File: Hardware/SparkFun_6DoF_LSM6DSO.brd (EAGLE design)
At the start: 25.4 x 25.4 mm, 62 parts, among them J1 QWIIC_RIGHT_ANGLE, J2 QWIIC_RIGHT_ANGLE, U1 LSM6DS0

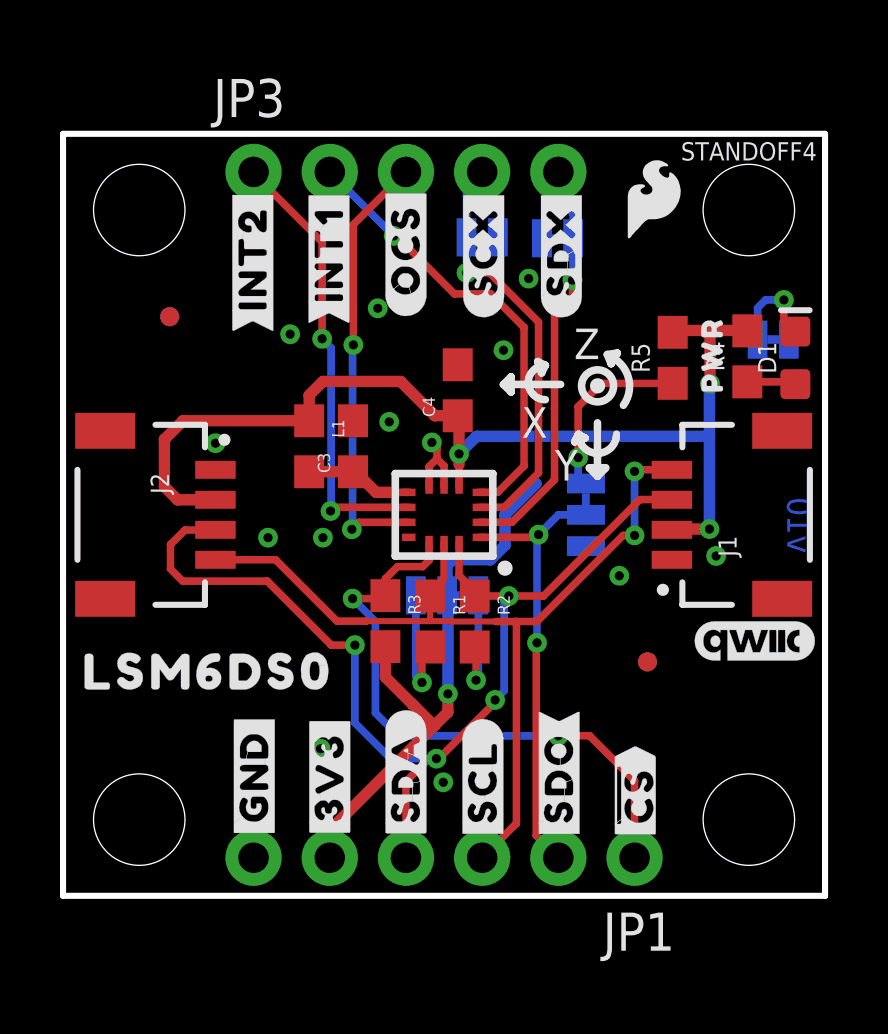
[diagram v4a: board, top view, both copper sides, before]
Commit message: Updates IC with production ID, adjusts connector section
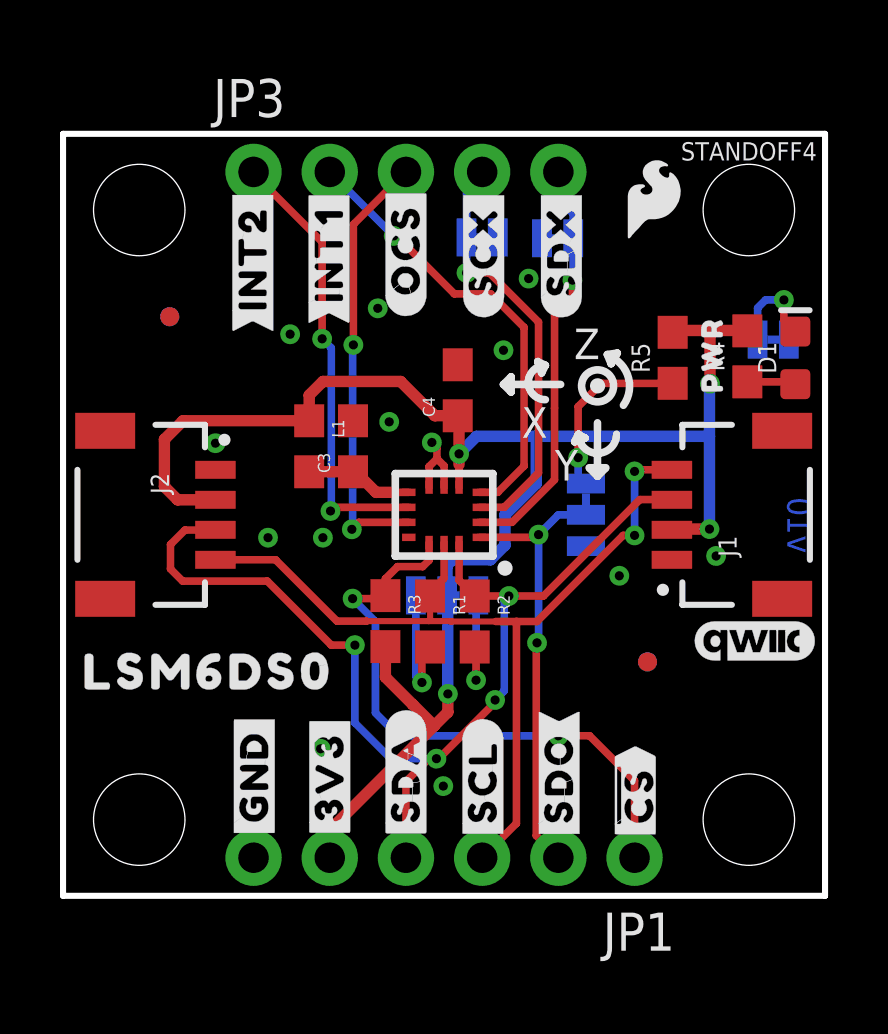
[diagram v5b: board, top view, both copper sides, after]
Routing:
- net 3.3V: track 56.1 -> 57.7 mm
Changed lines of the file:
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@@
 <setting verticaltext="up"/>
 </settings>
-<grid distance="0.05" unitdist="inch" unit="inch" style="dots" multiple="1" display="yes" altdistance="0.005" altunitdist="inch" altunit="inch"/>
+<grid distance="0.01" unitdist="inch" unit="inch" style="dots" multiple="1" display="yes" altdistance="0.001" altunitdist="inch" altunit="inch"/>
 <layers>
 <layer number="1" name="Top" color="4" fill="1" visible="yes" active="yes"/>
@@
 <element name="U1" library="temp" package="LGA14L" value="LSM6DS0" x="12.7" y="12.7" smashed="yes" rot="R180">
 <attribute name="NAME" x="14.057" y="10.928" size="0.6096" layer="27" font="vector" ratio="20" rot="R180"/>
+<attribute name="PROD_ID" value="IC-15837" x="12.7" y="12.7" size="1.778" layer="27" rot="R180" display="off"/>
 <attribute name="VALUE" x="14.311" y="15.091" size="0.6096" layer="27" font="vector" ratio="20" rot="R180"/>
 </element>
@@
 <wire x1="12.4634" y1="14.57056875" x2="12.4634" y2="14.9432" width="0.254" layer="1"/>
 <wire x1="12.4634" y1="14.9432" x2="12.2936" y2="15.113" width="0.254" layer="1"/>
-<via x="12.6746" y="3.7846" extent="1-16" drill="0.3048"/>
+<via x="12.6746" y="3.6576" extent="1-16" drill="0.3048"/>
 </signal>
 <signal name="VDD">
@@
 <wire x1="12.7" y1="10.58455" x2="12.23645" y2="10.121" width="0.254" layer="1"/>
 <wire x1="12.23645" y1="10.121" x2="12.23645" y2="9.994" width="0.254" layer="1"/>
-<wire x1="9.1322" y1="9.1558" x2="10.11225" y2="9.1558" width="0.254" layer="1"/>
-<wire x1="10.11225" y1="9.1558" x2="10.11315" y2="9.1567" width="0.254" layer="1"/>
 <wire x1="12.9422" y1="9.1558" x2="12.954" y2="9.144" width="0.2032" layer="1"/>
-<wire x1="10.16" y1="9.1558" x2="12.192" y2="9.1558" width="0.2032" layer="1"/>
 <wire x1="12.192" y1="9.1558" x2="12.9422" y2="9.1558" width="0.2032" layer="1"/>
 <wire x1="12.23645" y1="9.994" x2="12.23645" y2="9.20025" width="0.2032" layer="1"/>
+<wire x1="9.1322" y1="9.1558" x2="10.11225" y2="9.1558" width="0.254" layer="1"/>
+<wire x1="10.11315" y1="9.1567" x2="10.11225" y2="9.1558" width="0.254" layer="1"/>
 <wire x1="12.23645" y1="9.20025" x2="12.192" y2="9.1558" width="0.2032" layer="1"/>
-<wire x1="10.16" y1="9.1558" x2="10.11315" y2="9.1567" width="0" layer="19" extent="1-1"/>
+<wire x1="12.192" y1="9.1558" x2="10.11225" y2="9.1558" width="0.2032" layer="1"/>
 </signal>
 <signal name="SDA">
@@
 <contactref element="J1" pad="3"/>
 <contactref element="R2" pad="1"/>
-<wire x1="13.72235" y1="10.356846875" x2="13.72235" y2="10.16" width="0.254" layer="1"/>
-<wire x1="13.72235" y1="10.16" x2="13.72235" y2="9.994003125" width="0.254" layer="1"/>
-<wire x1="13.72235" y1="9.994" x2="14.859" y2="9.994" width="0.254" layer="1"/>
 <wire x1="14.859" y1="9.994" x2="16.0138" y2="9.994" width="0.254" layer="1"/>
 <wire x1="16.0138" y1="9.994" x2="19.2278" y2="13.208" width="0.254" layer="1"/>
@@
 <wire x1="8.9408" y1="8.3566" x2="6.8072" y2="10.4902" width="0.254" layer="1"/>
 <contactref element="U1" pad="14"/>
-<wire x1="13.2" y1="11.775" x2="13.2" y2="10.68235" width="0.254" layer="1"/>
-<wire x1="13.2" y1="10.68235" x2="13.72235" y2="10.16" width="0.254" layer="1"/>
 <wire x1="12.5222" y1="4.572" x2="14.3891" y2="6.4389" width="0.254" layer="1"/>
 <wire x1="12.192" y1="4.572" x2="11.43" y2="3.81" width="0.254" layer="1"/>
 <wire x1="11.43" y1="3.81" x2="11.43" y2="1.27" width="0.254" layer="1"/>
 <wire x1="12.446" y1="4.572" x2="12.192" y2="4.572" width="0.254" layer="1"/>
-<wire x1="13.72235" y1="9.994" x2="13.72235" y2="9.994003125" width="0" layer="19" extent="1-1"/>
+<wire x1="13.2" y1="10.51635" x2="13.2" y2="11.775" width="0.254" layer="1"/>
+<wire x1="14.859" y1="9.994" x2="13.72235" y2="9.994" width="0.254" layer="1"/>
+<wire x1="13.72235" y1="9.994" x2="13.2" y2="10.51635" width="0.254" layer="1"/>
 </signal>
 <signal name="!CS!">
@@
 <wire x1="16.51" y1="12.7" x2="17.43075" y2="12.7" width="0.254" layer="16"/>
 <wire x1="16.51" y1="1.27" x2="15.7734" y2="2.0066" width="0.254" layer="1"/>
+<via x="15.7988" y="8.4328" extent="1-16" drill="0.3048"/>
+<contactref element="U1" pad="1"/>
+<wire x1="13.875" y1="11.95" x2="15.76" y2="11.95" width="0.254" layer="1"/>
 <wire x1="15.7734" y1="2.0066" x2="15.7734" y2="8.4074" width="0.254" layer="1"/>
 <wire x1="15.7734" y1="8.4074" x2="15.7988" y2="8.4328" width="0.254" layer="1"/>
-<via x="15.7988" y="8.4328" extent="1-16" drill="0.3048"/>
-<wire x1="15.7988" y1="8.432803125" x2="15.7988" y2="11.9888" width="0.254" layer="16"/>
-<wire x1="15.7988" y1="11.9888" x2="15.8496" y2="12.0396" width="0.254" layer="16"/>
-<contactref element="U1" pad="1"/>
-<wire x1="13.875" y1="11.95" x2="15.76" y2="11.95" width="0.254" layer="1"/>
-<wire x1="15.7988" y1="8.4328" x2="15.7988" y2="8.432803125" width="0" layer="19" extent="16-16"/>
+<wire x1="15.8496" y1="12.0396" x2="15.8496" y2="8.4836" width="0.254" layer="16"/>
+<wire x1="15.8496" y1="8.4836" x2="15.7988" y2="8.4328" width="0.254" layer="16"/>
 </signal>
 <signal name="SDX">
@@
 <wire x1="22.8092" y1="18.8332" x2="22.7956" y2="18.8468" width="0.381" layer="1"/>
 <contactref element="U1" pad="5"/>
-<wire x1="13.2" y1="14.3764" x2="13.2" y2="13.625" width="0.254" layer="1"/>
-<wire x1="13.2" y1="14.732" x2="13.2" y2="14.3764" width="0.381" layer="1"/>
+<wire x1="13.2" y1="14.3764" x2="13.2" y2="14.732" width="0.381" layer="1"/>
 <wire x1="13.2" y1="14.732" x2="13.2" y2="15.9601" width="0.381" layer="1"/>
 <wire x1="13.2" y1="15.9601" x2="13.1572" y2="16.0029" width="0.381" layer="1"/>
 <wire x1="14.732" y1="12.7" x2="14.732" y2="11.684" width="0.381" layer="16"/>
 <wire x1="14.732" y1="11.684" x2="14.2494" y2="11.2014" width="0.381" layer="16"/>
-<wire x1="12.8016" y1="11.0236" x2="12.8016" y2="10.01395" width="0.381" layer="16"/>
-<wire x1="15.7734" y1="13.7414" x2="14.732" y2="12.7" width="0.381" layer="16"/>
+<wire x1="14.732" y1="12.7" x2="15.7734" y2="13.7414" width="0.381" layer="16"/>
 <wire x1="14.2494" y1="11.2014" x2="12.9794" y2="11.2014" width="0.381" layer="16"/>
 <wire x1="12.9794" y1="11.2014" x2="12.8016" y2="11.0236" width="0.381" layer="16"/>
@@
 <wire x1="21.5472" y1="12.2254" x2="21.5472" y2="15.3162" width="0.381" layer="16"/>
 <wire x1="13.7842" y1="15.3162" x2="13.2" y2="14.732" width="0.381" layer="16"/>
-<wire x1="13.7842" y1="15.3162" x2="21.5472" y2="15.3162" width="0.381" layer="16"/>
+<wire x1="13.7842" y1="15.3162" x2="15.748" y2="15.3162" width="0.381" layer="16"/>
+<wire x1="15.748" y1="15.3162" x2="21.5472" y2="15.3162" width="0.381" layer="16"/>
 <wire x1="21.5472" y1="17.0514" x2="21.5472" y2="15.3162" width="0.381" layer="16"/>
 <wire x1="21.5472" y1="17.0514" x2="21.5646" y2="17.0688" width="0.381" layer="16"/>
@@
 <wire x1="21.5646" y1="17.0688" x2="21.5646" y2="18.8214" width="0.381" layer="1"/>
 <wire x1="21.5646" y1="18.8214" x2="21.59" y2="18.8468" width="0.381" layer="1"/>
-<wire x1="12.827" y1="9.98855" x2="12.8016" y2="10.01395" width="0" layer="19" extent="16-16"/>
-<wire x1="13.2" y1="13.625" x2="15.7734" y2="13.7414" width="0" layer="19" extent="1-16"/>
+<wire x1="13.2" y1="13.625" x2="13.2" y2="14.3764" width="0.254" layer="1"/>
+<wire x1="15.7734" y1="13.7414" x2="15.7734" y2="15.2908" width="0.381" layer="16"/>
+<wire x1="15.7734" y1="15.2908" x2="15.748" y2="15.3162" width="0.381" layer="16"/>
+<wire x1="12.8016" y1="11.0236" x2="12.8016" y2="10.01395" width="0.381" layer="16"/>
+<wire x1="12.8016" y1="10.01395" x2="12.827" y2="9.98855" width="0.381" layer="16"/>
 </signal>
 <signal name="OCS">
@@
 <wire x1="13.72235" y1="8.294" x2="13.7668" y2="8.24955" width="0.254" layer="1"/>
 <via x="13.7668" y="7.1882" extent="1-16" drill="0.3048"/>
-<wire x1="13.843" y1="10.01395" x2="13.843" y2="7.2644" width="0.254" layer="16"/>
-<wire x1="13.7668" y1="7.1882" x2="13.843" y2="7.2644" width="0.254" layer="16"/>
 <wire x1="13.7668" y1="8.24955" x2="13.7668" y2="7.1882" width="0.254" layer="1"/>
+<wire x1="13.7668" y1="7.1882" x2="13.7668" y2="9.93775" width="0.254" layer="16"/>
+<wire x1="13.7668" y1="9.93775" x2="13.843" y2="10.01395" width="0.254" layer="16"/>
 </signal>
 <signal name="N$2">

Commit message: Adds SDO_AUX to header, updates symbol to have more consistent labeling
* Approves some minor DRC errors
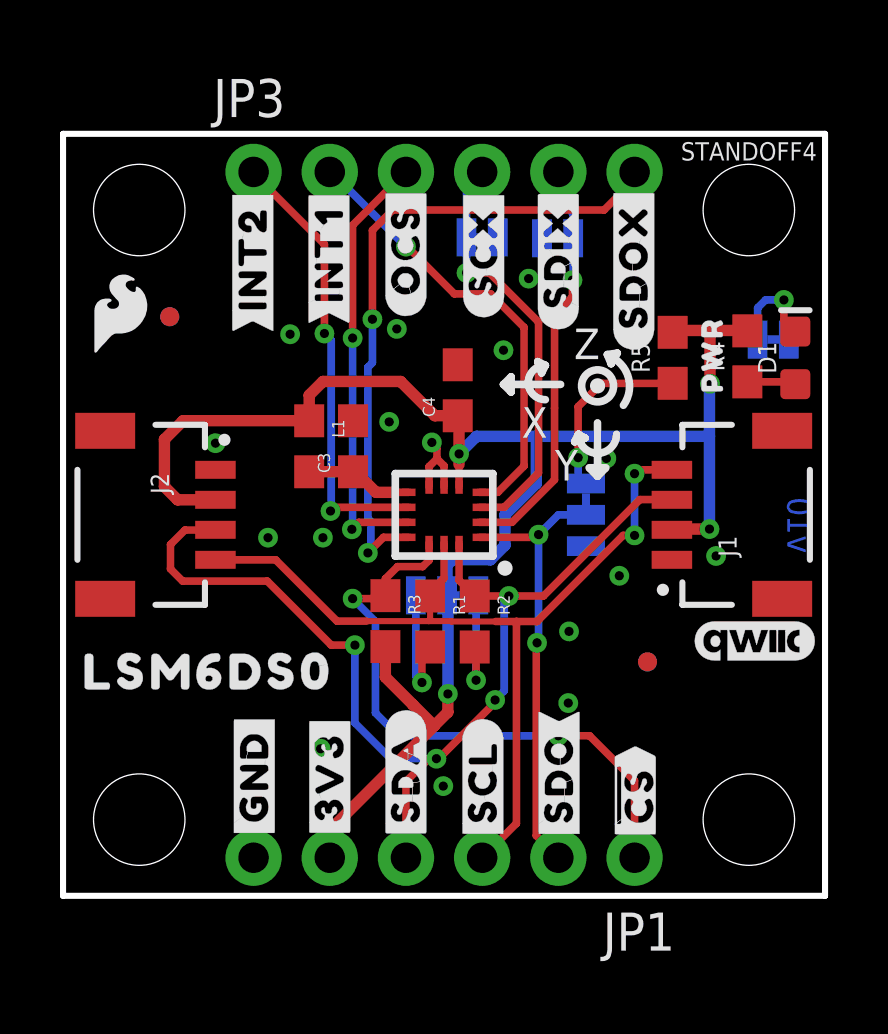
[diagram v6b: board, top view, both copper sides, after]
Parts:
- added U$32: (no value), bot:#SDOX#12
- added U$33: (no value), bot:#SDIX#11
- JP3: device SparkFun-Connectors:1X05_NO_SILK -> SparkFun-Connectors:1X06_NO_SILK
- U$11: device top:#SDX#10 -> top:#SDIX#11
- U$24: device bot:#SDX#9 -> top:#SDOX#12
- moved LOGO2 18.4 mm to (1.88, 18.6)
- moved U$29 18.2 mm to (1.91, 19.4)
- moved U$24 3.24 mm to (19.0, 21.0), flipped to the top, turned to 90 degrees
- moved U$11 0.20 mm to (16.5, 21.3)
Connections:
- net SDX renamed SDI_AUX
- new net SDO_AUX: JP3.6, U1.11
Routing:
- net SDO_AUX: track 0.00 -> 22.2 mm, vias 0 -> 2
- net SCL: track 31.1 -> 30.5 mm
- net GND: vias 13 -> 16
